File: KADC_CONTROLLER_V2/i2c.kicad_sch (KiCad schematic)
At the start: 13 parts, among them U43 PCA9306DCUR, U45 M24C64-DRDW8TP/K

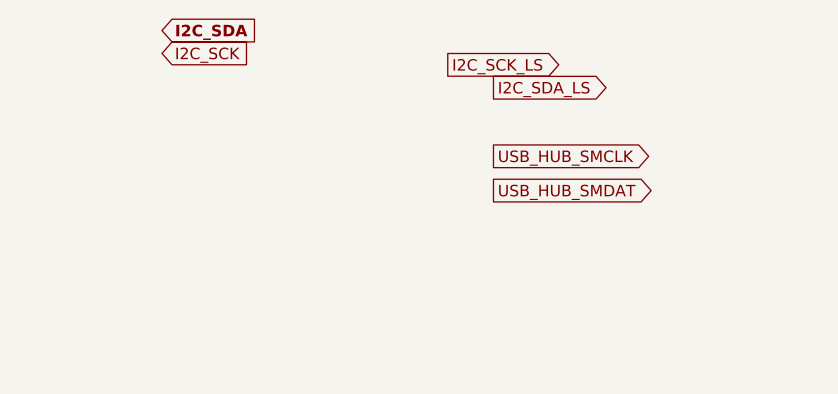
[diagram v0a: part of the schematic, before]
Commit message: Added footprints, updated schematic
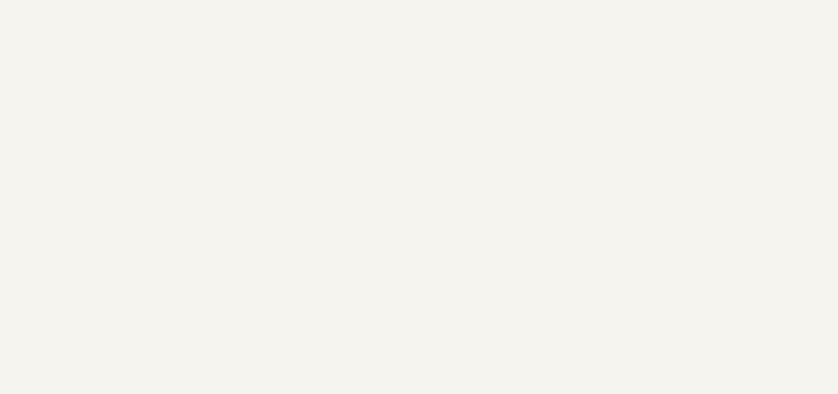
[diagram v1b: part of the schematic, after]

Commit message: Quick Updates, Power verification finalized
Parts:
- U43: footprint DCU8 -> PCA9306DCUR:DCU8
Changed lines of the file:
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@@
 			)
 		)
-		(property "Footprint" "DCU8"
+		(property "Footprint" "PCA9306DCUR:DCU8"
 			(at 444.246 53.34 0)
 			(hide yes)

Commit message: update
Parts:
- removed C194: 100p, Capacitor_SMD:C_0603_1608Metric, symbol Device:C_Small
- removed R175: 0R, symbol Device:R_Small_US
- added C249: 100p, Capacitor_SMD:C_0603_1608Metric, symbol Device:C_Small
- added R210: 0R, symbol Device:R_Small_US
- added TP44: EEPROM_WC_B, TestPoint:TestPoint_THTPad_1.5x1.5mm_Drill0.7mm, symbol Connector:TestPoint
- U45: footprint TSSOP8_4P5X3P1X0P65_STM -> M24C64_DRDW8TP:TSSOP8_4P5X3P1X0P65_STM
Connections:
- net EEPROM_WC_B: now also R210.2, TP44.1
- net GND: now also C249.2
- net PS_3V3: now also R176.2, U45.8 (VCC), C249.1; no longer R176.1, U45.7 (*WC)
- new net: R176.1, R210.1, U45.7 (*WC)

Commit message: sd changes, added connector for breakout board
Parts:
- R101, R146, R176, R210, R29, R44: footprint (none) -> Resistor_SMD:R_0603_1608Metric
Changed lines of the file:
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@@
 			)
 		)
-		(property "Footprint" ""
+		(property "Footprint" "Resistor_SMD:R_0603_1608Metric"
 			(at 506.73 49.53 0)
 			(hide yes)
@@
 			)
 		)
-		(property "Footprint" ""
+		(property "Footprint" "Resistor_SMD:R_0603_1608Metric"
 			(at 497.84 49.53 0)
 			(hide yes)
@@
 			)
 		)
-		(property "Footprint" ""
+		(property "Footprint" "Resistor_SMD:R_0603_1608Metric"
 			(at 152.4 67.31 0)
 			(hide yes)
@@
 			)
 		)
-		(property "Footprint" ""
+		(property "Footprint" "Resistor_SMD:R_0603_1608Metric"
 			(at 523.24 82.55 0)
 			(hide yes)
@@
 			)
 		)
-		(property "Footprint" ""
+		(property "Footprint" "Resistor_SMD:R_0603_1608Metric"
 			(at 487.68 49.53 0)
 			(hide yes)
@@
 			)
 		)
-		(property "Footprint" ""
+		(property "Footprint" "Resistor_SMD:R_0603_1608Metric"
 			(at 160.02 76.2 0)
 			(hide yes)

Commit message: SD connector added
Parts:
- R145: footprint (none) -> Resistor_SMD:R_0603_1608Metric
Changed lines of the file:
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@@
 			)
 		)
-		(property "Footprint" ""
+		(property "Footprint" "Resistor_SMD:R_0603_1608Metric"
 			(at 523.24 78.74 0)
 			(hide yes)

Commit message: quick update
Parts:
- added TP45: EEPROM_GND, TestPoint:TestPoint_THTPad_1.5x1.5mm_Drill0.7mm, symbol Connector:TestPoint
- C249: value 100p -> 0.1u
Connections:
- net GND: now also TP45.1
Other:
- note added: "TIE TP44 to TP45 Via a Jumper to write to EEPROM"
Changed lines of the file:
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@@
+		)
+	)
+	(text "TIE TP44 to TP45\nVia a Jumper to write to EEPROM"
+		(exclude_from_sim no)
+		(at 184.912 90.17 0)
+		(effects
+			(font
+				(size 1.27 1.27)
+			)
 		)
 	)
@@
 		(pts
 			(xy 140.97 58.42) (xy 152.4 58.42)
+		)
+		(stroke
+			(width 0)
+			(type default)
+		)
+	)
+	(wire
+		(pts
+			(xy 165.1 85.09) (xy 165.1 91.44)
 		)
 		(stroke
@@
 	)
 	(symbol
+		(lib_id "power:GND")
+		(at 165.1 91.44 0)
+		(unit 1)
+		(body_style 1)
+		(exclude_from_sim no)
+		(in_bom yes)
+		(on_board yes)
+		(in_pos_files yes)
+		(dnp no)
+		(fields_autoplaced yes)
+		(property "Reference" "#PWR0134"
+			(at 165.1 97.79 0)
+			(hide yes)
+			(show_name no)
+			(do_not_autoplace no)
+			(effects
+				(font
+					(size 1.27 1.27)
+				)
+			)
+		)
+		(property "Value" "GND"
+			(at 165.1 96.52 0)
+			(show_name no)
+			(do_not_autoplace no)
+			(effects
+				(font
+					(size 1.27 1.27)
+				)
+			)
+		)
+		(property "Footprint" ""
+			(at 165.1 91.44 0)
+			(hide yes)
+			(show_name no)
+			(do_not_autoplace no)
+			(effects
+				(font
+					(size 1.27 1.27)
+				)
+			)
+		)
+		(property "Datasheet" ""
+			(at 165.1 91.44 0)
+			(hide yes)
+			(show_name no)
+			(do_not_autoplace no)
+			(effects
+				(font
+					(size 1.27 1.27)
+				)
+			)
+		)
+		(property "Description" "Power symbol creates a global label with name \"GND\" , ground"
+			(at 165.1 91.44 0)
+			(hide yes)
+			(show_name no)
+			(do_not_autoplace no)
+			(effects
+				(font
+					(size 1.27 1.27)
+				)
+			)
+		)
+		(pin "1"
+		)
+		(instances
+			(project "PSEC5_Ctrl_Board"
+				(path "/165f2ae6-d522-4adf-a6c4-bb137b209d33/1f6d7a03-cfad-4370-8d2b-49ab19e248d8/8fe5b1b9-ced8-42bc-a674-ead32ce92914"
+					(reference "#PWR0134")
+					(unit 1)
+				)
+			)
+		)
+	)
+	(symbol
 		(lib_id "Device:R_Small_US")
 		(at 497.84 49.53 0)
@@
 	)
 	(symbol
+		(lib_id "Connector:TestPoint")
+		(at 165.1 85.09 0)
+		(unit 1)
+		(body_style 1)
+		(exclude_from_sim no)
+		(in_bom yes)
+		(on_board yes)
+		(in_pos_files yes)
+		(dnp no)
+		(fields_autoplaced yes)
+		(property "Reference" "TP45"
+			(at 167.64 80.5179 0)
+			(show_name no)
+			(do_not_autoplace no)
+			(effects
+				(font
+					(size 1.27 1.27)
+				)
+				(justify left)
+			)
+		)
+		(property "Value" "EEPROM_GND"
+			(at 167.64 83.0579 0)
+			(show_name no)
+			(do_not_autoplace no)
+			(effects
+				(font
+					(size 1.27 1.27)
+				)
+				(justify left)
+			)
+		)
+		(property "Footprint" "TestPoint:TestPoint_THTPad_1.5x1.5mm_Drill0.7mm"
+			(at 170.18 85.09 0)
+			(hide yes)
+			(show_name no)
+			(do_not_autoplace no)
+			(effects
+				(font
+					(size 1.27 1.27)
+				)
+			)
+		)
+		(property "Datasheet" ""
+			(at 170.18 85.09 0)
+			(hide yes)
+			(show_name no)
+			(do_not_autoplace no)
+			(effects
+				(font
+					(size 1.27 1.27)
+				)
+			)
+		)
+		(property "Description" "test point"
+			(at 165.1 85.09 0)
+			(hide yes)
+			(show_name no)
+			(do_not_autoplace no)
+			(effects
+				(font
+					(size 1.27 1.27)
+				)
+			)
+		)
+		(pin "1"
+		)
+		(instances
+			(project "PSEC5_Ctrl_Board"
+				(path "/165f2ae6-d522-4adf-a6c4-bb137b209d33/1f6d7a03-cfad-4370-8d2b-49ab19e248d8/8fe5b1b9-ced8-42bc-a674-ead32ce92914"
+					(reference "TP45")
+					(unit 1)
+				)
+			)
+		)
+	)
+	(symbol
 		(lib_id "Device:C_Small")
 		(at 203.2 69.85 0)
@@
 			)
 		)
-		(property "Value" "100p"
+		(property "Value" "0.1u"
 			(at 196.088 70.612 0)
 			(show_name no)

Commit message: usb changes
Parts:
- R145, R146: value 0R -> DNP
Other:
- note added: "DNP for initial startup Use 0R for future firmware programming of USB hub"
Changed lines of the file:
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@@
+		)
+	)
+	(text "DNP for initial startup\nUse 0R for future firmware\nprogramming of USB hub"
+		(exclude_from_sim no)
+		(at 523.494 90.932 0)
+		(effects
+			(font
+				(size 1.27 1.27)
+			)
 		)
 	)
@@
 			)
 		)
-		(property "Value" "0R"
+		(property "Value" "DNP"
 			(at 526.034 77.216 90)
 			(show_name no)
@@
 			)
 		)
-		(property "Value" "0R"
+		(property "Value" "DNP"
 			(at 526.034 81.026 90)
 			(show_name no)
